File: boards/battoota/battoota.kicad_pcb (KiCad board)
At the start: 2 copper layers, 122.6 x 88.9 mm, 38 parts

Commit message: battoota clean up
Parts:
- removed S10, S12, S14, S16, S18, S20, S22, S24, S28, S30, S32, S34, S4, S6, S8: , PG1350
- S11, S13, S15, S17, S19, S21, S23, S27, S29, S3, S31, S33, S5, S7, S9: footprint PG1350 -> Alaa:choc_hotswap_key
- moved S27 1.72 mm to (133.6, -78.5)
- moved S29 1.72 mm to (133.6, -95.5)
- moved S19 1.61 mm to (115.4, -71.1)
- moved S21 1.61 mm to (115.4, -88.1)
- moved S23 1.61 mm to (115.4, -105.1)
- moved REF** 1.50 mm to (103.8, -86.6)
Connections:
- S11 pad : P3 -> (no net)
- S13 pad : P2 -> (no net)
- S27 pad : P19 -> (no net)
- S29 pad : P20 -> (no net)
- S7 pad : P5 -> (no net)
- S9 pad : P4 -> (no net)
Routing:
- net P2: track 131.6 -> 134.3 mm
- net P15: track 150.2 -> 152.9 mm
- net P18: track 136.7 -> 139.4 mm
- net P16: track 96.8 -> 95.1 mm
- net P20: track 43.9 -> 45.6 mm
- net P10: track 109.7 -> 108.1 mm
- net P7: track 159.0 -> 160.5 mm
- net P6: track 178.1 -> 179.6 mm
- net P4: track 152.4 -> 153.9 mm
- net P3: track 172.1 -> 173.6 mm
- net P5: track 141.4 -> 142.9 mm
- net P19: track 57.7 -> 58.9 mm
- added copper zone on F.Cu, net (none)

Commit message: clean up all the boards
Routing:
- net GND: track 286.0 -> 30.6 mm
- added copper zone on F.Cu, net GND
- removed copper zone on F.Cu, net (none)
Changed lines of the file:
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@@
   (segment (start 47.655954 -88.184596) (end 48.856953 -86.983597) (width 0.25) (layer "B.Cu") (net 1))
   (segment (start 48.856953 -86.983597) (end 48.856953 -78.356283) (width 0.25) (layer "B.Cu") (net 1))
-  (segment (start 122.409791 -55.455499) (end 122.889627 -55.935335) (width 0.5) (layer "F.Cu") (net 2))
-  (segment (start 141.459791 -49.809121) (end 143.680465 -52.029795) (width 0.5) (layer "F.Cu") (net 2))
-  (segment (start 108.167264 -73.809781) (end 107.149791 -74.827254) (width 0.5) (layer "F.Cu") (net 2))
-  (segment (start 63.384822 -105.421809) (end 62.586645 -106.219986) (width 0.5) (layer "F.Cu") (net 2))
-  (segment (start 96.21751 -74.301308) (end 89.760656 -74.301308) (width 0.5) (layer "F.Cu") (net 2))
-  (segment (start 133.599495 -89.644491) (end 127.233116 -89.644491) (width 0.5) (layer "F.Cu") (net 2))
-  (segment (start 63.384822 -100.80225) (end 63.384822 -105.421809) (width 0.5) (layer "F.Cu") (net 2))
-  (segment (start 127.872013 -72.644491) (end 125.324495 -75.192009) (width 0.5) (layer "F.Cu") (net 2))
-  (segment (start 75.363653 -82.192969) (end 74.347654 -81.17697) (width 0.5) (layer "F.Cu") (net 2))
-  (segment (start 115.424791 -65.177254) (end 109.829464 -65.177254) (width 0.5) (layer "F.Cu") (net 2))
-  (segment (start 125.324495 -91.553112) (end 125.324495 -99.294491) (width 0.5) (layer "F.Cu") (net 2))
-  (segment (start 108.167264 -66.839454) (end 108.167264 -73.809781) (width 0.5) (layer "F.Cu") (net 2))
-  (segment (start 62.586645 -106.219986) (end 62.586645 -107.001157) (width 0.5) (layer "F.Cu") (net 2))
-  (segment (start 66.26837 -97.918702) (end 63.384822 -100.80225) (width 0.5) (layer "F.Cu") (net 2))
-  (segment (start 74.347654 -81.17697) (end 68.485407 -81.17697) (width 0.5) (layer "F.Cu") (net 2))
-  (segment (start 71.813295 -64.435238) (end 68.490683 -67.75785) (width 0.5) (layer "F.Cu") (net 2))
-  (segment (start 141.459791 -42.698254) (end 141.459791 -49.809121) (width 0.5) (layer "F.Cu") (net 2))
-  (segment (start 89.760656 -74.301308) (end 87.132946 -76.929018) (width 0.5) (layer "F.Cu") (net 2))
-  (segment (start 109.829464 -65.177254) (end 108.167264 -66.839454) (width 0.5) (layer "F.Cu") (net 2))
-  (segment (start 49.917361 -65.987885) (end 48.802762 -67.102484) (width 0.5) (layer "F.Cu") (net 2))
-  (segment (start 59.537571 -60.830584) (end 58.196209 -59.489222) (width 0.5) (layer "F.Cu") (net 2))
-  (segment (start 77.299673 -64.435238) (end 71.813295 -64.435238) (width 0.5) (layer "F.Cu") (net 2))
-  (segment (start 115.424791 -82.177254) (end 108.987449 -82.177254) (width 0.5) (layer "F.Cu") (net 2))
-  (segment (start 124.609447 -44.744455) (end 122.409791 -46.944111) (width 0.5) (layer "F.Cu") (net 2))
-  (segment (start 78.315672 -65.451237) (end 77.299673 -64.435238) (width 0.5) (layer "F.Cu") (net 2))
-  (segment (start 58.196209 -59.489222) (end 53.137791 -59.489222) (width 0.5) (layer "F.Cu") (net 2))
-  (segment (start 71.395635 -97.918702) (end 66.26837 -97.918702) (width 0.5) (layer "F.Cu") (net 2))
-  (segment (start 53.137791 -59.489222) (end 49.917361 -62.709652) (width 0.5) (layer "F.Cu") (net 2))
-  (segment (start 115.424791 -99.177254) (end 109.579975 -99.177254) (width 0.5) (layer "F.Cu") (net 2))
-  (segment (start 133.599495 -72.644491) (end 127.872013 -72.644491) (width 0.5) (layer "F.Cu") (net 2))
-  (segment (start 86.601289 -108.171928) (end 86.570217 -108.140856) (width 0.5) (layer "F.Cu") (net 2))
-  (segment (start 93.254215 -108.171928) (end 86.601289 -108.171928) (width 0.5) (layer "F.Cu") (net 2))
-  (segment (start 68.485407 -81.17697) (end 65.538664 -84.123713) (width 0.5) (layer "F.Cu") (net 2))
-  (segment (start 85.651298 -93.599163) (end 85.651298 -100.128683) (width 0.5) (layer "F.Cu") (net 2))
-  (segment (start 65.538664 -84.123713) (end 65.538664 -90.259425) (width 0.5) (layer "F.Cu") (net 2))
-  (segment (start 48.802762 -67.102484) (end 48.802762 -67.639549) (width 0.5) (layer "F.Cu") (net 2))
-  (segment (start 147.315045 -39.848335) (end 144.30971 -39.848335) (width 0.5) (layer "F.Cu") (net 2))
   (segment (start 154.256703 -110.643254) (end 150.44369 -110.643254) (width 0.5) (layer "F.Cu") (net 2))
-  (segment (start 122.409791 -46.944111) (end 122.409791 -55.455499) (width 0.5) (layer "F.Cu") (net 2))
-  (segment (start 108.167264 -74.406264) (end 107.149791 -75.423737) (width 0.5) (layer "F.Cu") (net 2))
-  (segment (start 109.579975 -99.177254) (end 107.14979 -101.607439) (width 0.5) (layer "F.Cu") (net 2))
-  (segment (start 94.735862 -91.236618) (end 88.013843 -91.236618) (width 0.5) (layer "F.Cu") (net 2))
-  (segment (start 48.232895 -75.218284) (end 44.864298 -78.586881) (width 0.5) (layer "F.Cu") (net 2))
-  (segment (start 87.132946 -76.929018) (end 87.132946 -83.193373) (width 0.5) (layer "F.Cu") (net 2))
-  (segment (start 129.187964 -44.744455) (end 124.609447 -44.744455) (width 0.5) (layer "F.Cu") (net 2))
-  (segment (start 88.013843 -91.236618) (end 85.651298 -93.599163) (width 0.5) (layer "F.Cu") (net 2))
-  (segment (start 108.987449 -82.177254) (end 107.149791 -84.014912) (width 0.5) (layer "F.Cu") (net 2))
   (segment (start 154.304587 -110.691138) (end 154.256703 -110.643254) (width 0.5) (layer "F.Cu") (net 2))
-  (segment (start 127.233116 -89.644491) (end 125.324495 -91.553112) (width 0.5) (layer "F.Cu") (net 2))
-  (segment (start 44.864298 -78.586881) (end 44.864298 -82.864875) (width 0.5) (layer "F.Cu") (net 2))
-  (segment (start 86.570217 -108.140856) (end 84.169651 -110.541422) (width 0.5) (layer "F.Cu") (net 2))
-  (segment (start 144.30971 -39.848335) (end 141.459791 -42.698254) (width 0.5) (layer "F.Cu") (net 2))
-  (segment (start 54.567252 -77.087765) (end 52.697771 -75.218284) (width 0.5) (layer "F.Cu") (net 2))
-  (segment (start 72.411634 -98.934701) (end 71.395635 -97.918702) (width 0.5) (layer "F.Cu") (net 2))
-  (segment (start 107.149791 -84.014912) (end 107.14979 -91.827254) (width 0.5) (layer "F.Cu") (net 2))
-  (segment (start 68.490683 -67.75785) (end 68.490683 -73.517693) (width 0.5) (layer "F.Cu") (net 2))
-  (segment (start 52.697771 -75.218284) (end 48.232895 -75.218284) (width 0.5) (layer "F.Cu") (net 2))
-  (segment (start 44.864298 -82.864875) (end 43.832443 -83.89673) (width 0.5) (layer "F.Cu") (net 2))
-  (segment (start 49.917361 -62.709652) (end 49.917361 -65.987885) (width 0.5) (layer "F.Cu") (net 2))
-  (segment (start 129.553156 -45.109647) (end 129.187964 -44.744455) (width 0.5) (layer "F.Cu") (net 2))
-  (segment (start 125.324495 -75.192009) (end 125.324495 -82.294491) (width 0.5) (layer "F.Cu") (net 2))
-  (segment (start 107.14979 -101.607439) (end 107.14979 -108.827254) (width 0.5) (layer "F.Cu") (net 2))
-  (segment (start 84.169651 -110.541422) (end 84.169651 -117.063993) (width 0.5) (layer "F.Cu") (net 2))
   (via (at 154.304587 -110.691138) (size 0.8) (drill 0.4) (layers "F.Cu" "B.Cu") (free) (net 2))
   (segment (start 154.329345 -110.66638) (end 154.352471 -110.643254) (width 0.5) (layer "B.Cu") (net 2))
@@
   (segment (start 135.118406 -112.746869) (end 135.109791 -112.738254) (width 0.5) (layer "B.Cu") (net 20))
   (segment (start 135.118406 -118.676838) (end 135.118406 -112.746869) (width 0.5) (layer "B.Cu") (net 20))
-  (zone (net 0) (net_name "") (layer "F.Cu") (hatch edge 0.508)
+  (zone (net 2) (net_name "GND") (layer "F.Cu") (hatch edge 0.508)
     (connect_pads (clearance 0.508))
     (min_thickness 0.254) (filled_areas_thickness no)
-    (fill yes (thermal_gap 0.508) (thermal_bridge_width 0.508))
+    (fill yes (thermal_gap 0.508) (thermal_bridge_width 0.508) (island_removal_mode 1) (island_area_min 0))
     (polygon
       (pts

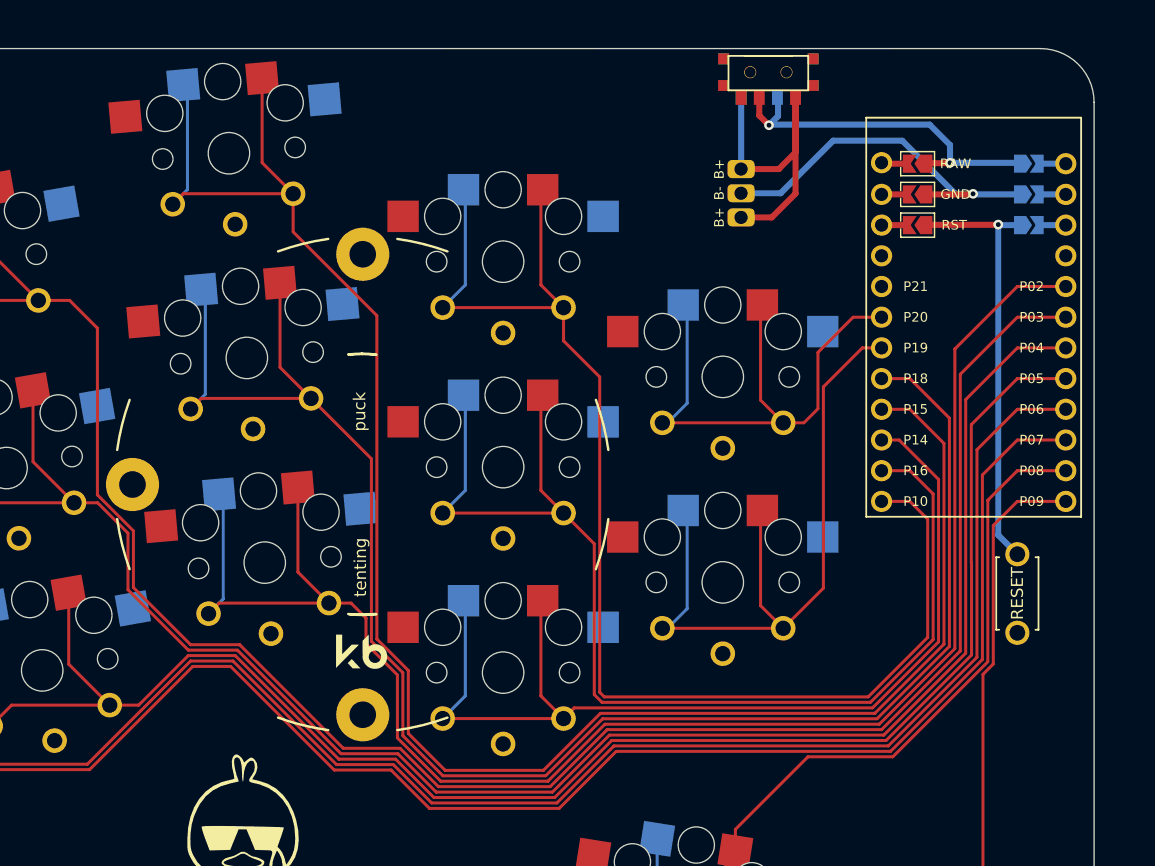
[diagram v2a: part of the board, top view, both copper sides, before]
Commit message: move mcu on battoota up
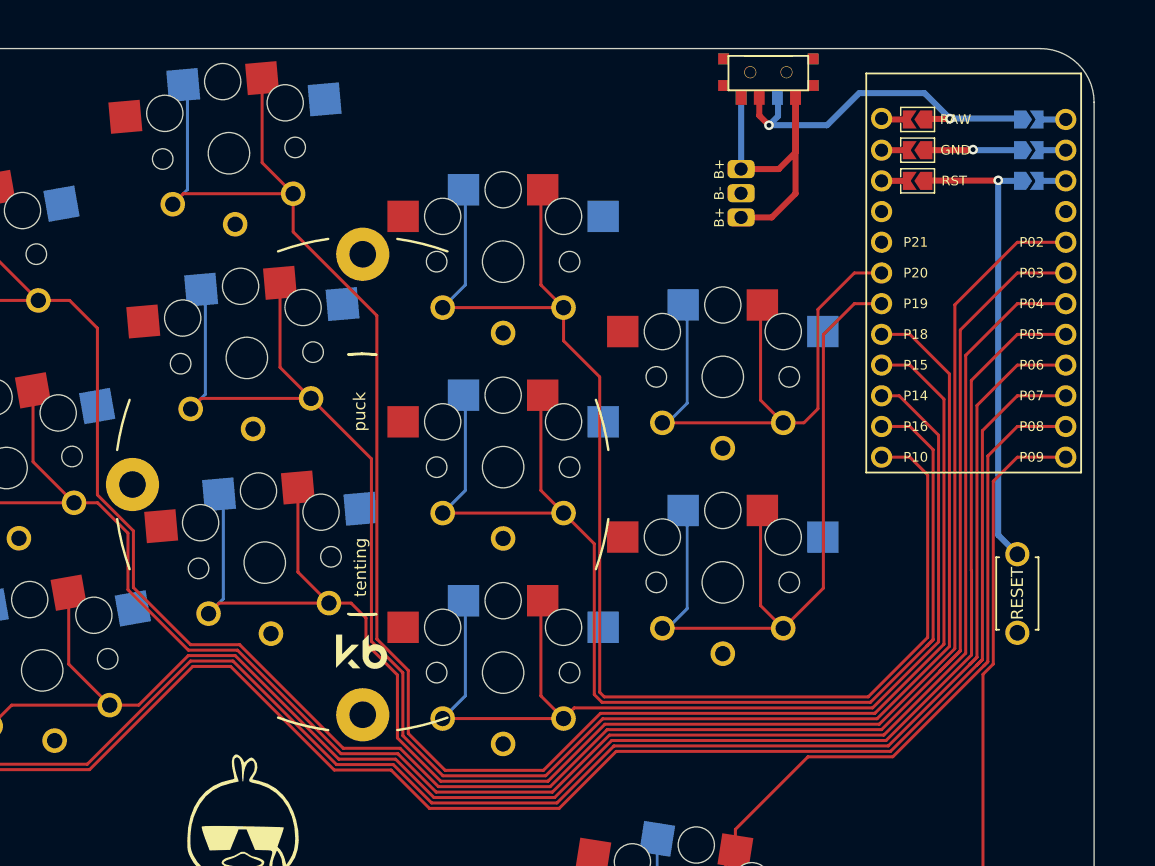
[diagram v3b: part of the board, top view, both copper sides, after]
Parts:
- moved MCU1 3.66 mm to (154.4, -102.9)
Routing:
- net GND: track 30.6 -> 7.75 mm
- net P3: track 173.6 -> 179.7 mm
- net P6: track 179.6 -> 184.0 mm
- net P16: track 95.1 -> 99.5 mm
- net P7: track 160.5 -> 164.9 mm
- net P8: track 81.1 -> 85.3 mm
- net P19: track 58.9 -> 63.0 mm
- net P4: track 153.9 -> 157.5 mm
- net P9: track 73.0 -> 76.7 mm
- net P2: track 134.3 -> 138.0 mm
- net P10: track 108.1 -> 111.8 mm
- net RST: track 35.7 -> 39.4 mm
- net P14: track 84.7 -> 88.3 mm
- net P5: track 142.9 -> 146.5 mm
- net P18: track 139.4 -> 143.1 mm
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
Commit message: min changes
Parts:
- moved G*** 10.0 mm to (103.8, -55.9)
- moved G*** 10.0 mm to (104.0, -55.9)
- moved S31 1.00 mm to (129.5, -50.9)
- moved S33 1.00 mm to (148.7, -45.2)
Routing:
- net P8: track 85.3 -> 88.3 mm
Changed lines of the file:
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@@
   )
   (footprint "LOGO" (layer "F.Cu")
-    (at 93.819755 -55.859733)
+    (at 103.819755 -55.859733)
     (attr board_only exclude_from_pos_files exclude_from_bom)
     (fp_text reference "G***" (at 0 0) (layer "F.SilkS") hide
@@
   )
   (footprint "Alaa:choc_hotswap_key" (layer "F.Cu")
-    (at 149.714791 -45.238254 -24)
+    (at 148.714791 -45.238254 -24)
     (attr through_hole)
     (fp_text reference "S33" (at 0 0 139) (layer "F.SilkS") hide
@@
   )
   (footprint "Alaa:choc_hotswap_key" (layer "F.Cu")
-    (at 130.476118 -50.937009 -9)
+    (at 129.476118 -50.937009 -9)
     (attr through_hole)
     (fp_text reference "S31" (at 0 0 154) (layer "F.SilkS") hide
@@
   )
   (footprint "LOGO" (layer "B.Cu")
-    (at 93.98 -55.88 180)
+    (at 103.98 -55.88 180)
     (attr board_only exclude_from_pos_files exclude_from_bom)
     (fp_text reference "G***" (at 0 0) (layer "B.SilkS") hide
@@
   (segment (start 155.527414 -71.97371) (end 155.191874 -71.638171) (width 0.25) (layer "F.Cu") (net 16))
   (segment (start 161.977213 -91.442348) (end 157.969791 -91.442348) (width 0.25) (layer "F.Cu") (net 16))
-  (segment (start 134.820109 -47.432936) (end 134.820109 -46.401621) (width 0.25) (layer "F.Cu") (net 16))
-  (segment (start 133.839791 -48.413254) (end 134.820109 -47.432936) (width 0.25) (layer "F.Cu") (net 16))
-  (segment (start 125.130937 -47.778254) (end 124.943226 -47.965965) (width 0.25) (layer "F.Cu") (net 16))
+  (segment (start 135.441288 -64.111751) (end 134.641581 -63.312044) (width 0.25) (layer "F.Cu") (net 16))
+  (segment (start 133.820109 -47.432936) (end 133.820109 -46.401621) (width 0.25) (layer "F.Cu") (net 16))
+  (segment (start 132.839791 -48.413254) (end 133.820109 -47.432936) (width 0.25) (layer "F.Cu") (net 16))
+  (segment (start 124.130937 -47.778254) (end 123.943226 -47.965965) (width 0.25) (layer "F.Cu") (net 16))
+  (segment (start 155.191874 -71.638171) (end 147.665453 -64.111751) (width 0.25) (layer "F.Cu") (net 16))
   (segment (start 155.527414 -71.973711) (end 155.191874 -71.638171) (width 0.25) (layer "F.Cu") (net 16))
-  (segment (start 147.665453 -64.111751) (end 140.648288 -64.111751) (width 0.25) (layer "F.Cu") (net 16))
+  (segment (start 134.641581 -63.312044) (end 134.641581 -56.301431) (width 0.25) (layer "F.Cu") (net 16))
   (segment (start 155.527414 -88.999971) (end 155.527414 -71.973711) (width 0.25) (layer "F.Cu") (net 16))
-  (segment (start 134.820109 -46.401621) (end 133.443476 -47.778254) (width 0.25) (layer "F.Cu") (net 16))
-  (segment (start 140.648288 -64.111751) (end 134.641582 -58.105045) (width 0.25) (layer "F.Cu") (net 16))
-  (segment (start 133.443476 -47.778254) (end 125.130937 -47.778254) (width 0.25) (layer "F.Cu") (net 16))
+  (segment (start 133.820109 -46.401621) (end 132.443476 -47.778254) (width 0.25) (layer "F.Cu") (net 16))
+  (segment (start 132.443476 -47.778254) (end 124.130937 -47.778254) (width 0.25) (layer "F.Cu") (net 16))
   (segment (start 134.641583 -56.301431) (end 133.839791 -55.499639) (width 0.25) (layer "F.Cu") (net 16))
-  (segment (start 133.839791 -55.499639) (end 133.839791 -48.413254) (width 0.25) (layer "F.Cu") (net 16))
-  (segment (start 134.641582 -58.105045) (end 134.641582 -56.301432) (width 0.25) (layer "F.Cu") (net 16))
-  (segment (start 155.191874 -71.638171) (end 147.665453 -64.111751) (width 0.25) (layer "F.Cu") (net 16))
+  (segment (start 147.665453 -64.111751) (end 135.441288 -64.111751) (width 0.25) (layer "F.Cu") (net 16))
+  (segment (start 132.839791 -55.499639) (end 132.839791 -48.413254) (width 0.25) (layer "F.Cu") (net 16))
   (segment (start 157.969791 -91.442348) (end 155.527414 -88.999971) (width 0.25) (layer "F.Cu") (net 16))
-  (segment (start 124.943226 -49.041689) (end 124.943226 -47.965965) (width 0.25) (layer "B.Cu") (net 16))
-  (segment (start 128.172224 -52.270687) (end 124.943226 -49.041689) (width 0.25) (layer "B.Cu") (net 16))
-  (segment (start 128.172224 -57.326077) (end 128.172224 -52.270687) (width 0.25) (layer "B.Cu") (net 16))
-  (segment (start 155.976934 -71.787512) (end 155.126735 -70.937314) (width 0.25) (layer "F.Cu") (net 17))
-  (segment (start 152.889791 -39.88597) (end 152.736919 -39.733098) (width 0.25) (layer "F.Cu") (net 17))
-  (segment (start 152.889791 -47.104843) (end 152.889791 -39.88597) (width 0.25) (layer "F.Cu") (net 17))
-  (segment (start 155.976934 -86.909491) (end 155.976934 -71.787512) (width 0.25) (layer "F.Cu") (net 17))
-  (segment (start 150.774947 -39.733098) (end 146.707581 -43.800464) (width 0.25) (layer "F.Cu") (net 17))
-  (segment (start 152.736919 -39.733098) (end 150.774947 -39.733098) (width 0.25) (layer "F.Cu") (net 17))
-  (segment (start 146.707581 -43.800464) (end 143.601465 -43.800464) (width 0.25) (layer "F.Cu") (net 17))
+  (segment (start 123.943226 -49.041689) (end 123.943226 -47.965965) (width 0.25) (layer "B.Cu") (net 16))
+  (segment (start 127.172224 -52.270687) (end 123.943226 -49.041689) (width 0.25) (layer "B.Cu") (net 16))
+  (segment (start 127.172224 -57.326077) (end 127.172224 -52.270687) (width 0.25) (layer "B.Cu") (net 16))
+  (segment (start 151.889791 -39.88597) (end 151.736919 -39.733098) (width 0.25) (layer "F.Cu") (net 17))
   (segment (start 161.977213 -88.902348) (end 157.969791 -88.902348) (width 0.25) (layer "F.Cu") (net 17))
-  (segment (start 155.126735 -70.937314) (end 155.126735 -49.341787) (width 0.25) (layer "F.Cu") (net 17))
+  (segment (start 151.889791 -47.104843) (end 151.889791 -39.88597) (width 0.25) (layer "F.Cu") (net 17))
+  (segment (start 149.774947 -39.733098) (end 145.707581 -43.800464) (width 0.25) (layer "F.Cu") (net 17))
+  (segment (start 155.976934 -51.191986) (end 154.126734 -49.341786) (width 0.25) (layer "F.Cu") (net 17))
+  (segment (start 151.736919 -39.733098) (end 149.774947 -39.733098) (width 0.25) (layer "F.Cu") (net 17))
+  (segment (start 145.707581 -43.800464) (end 142.601465 -43.800464) (width 0.25) (layer "F.Cu") (net 17))
   (segment (start 157.969791 -88.902348) (end 155.976934 -86.909491) (width 0.25) (layer "F.Cu") (net 17))
-  (segment (start 155.126735 -49.341787) (end 152.889791 -47.104843) (width 0.25) (layer "F.Cu") (net 17))
-  (segment (start 149.143013 -52.005911) (end 149.143013 -49.746476) (width 0.25) (layer "B.Cu") (net 17))
-  (segment (start 149.143013 -49.746476) (end 143.601465 -44.204928) (width 0.25) (layer "B.Cu") (net 17))
-  (segment (start 143.601465 -44.204928) (end 143.601465 -43.800464) (width 0.25) (layer "B.Cu") (net 17))
+  (segment (start 154.126735 -49.341787) (end 151.889791 -47.104843) (width 0.25) (layer "F.Cu") (net 17))
+  (segment (start 155.976934 -86.909491) (end 155.976934 -51.191986) (width 0.25) (layer "F.Cu") (net 17))
+  (segment (start 148.143013 -52.005911) (end 148.143013 -49.746476) (width 0.25) (layer "B.Cu") (net 17))
+  (segment (start 148.143013 -49.746476) (end 142.601465 -44.204928) (width 0.25) (layer "B.Cu") (net 17))
+  (segment (start 142.601465 -44.204928) (end 142.601465 -43.800464) (width 0.25) (layer "B.Cu") (net 17))
   (segment (start 152.372041 -116.88499) (end 150.419502 -116.88499) (width 0.5) (layer "F.Cu") (net 18))
   (segment (start 136.618406 -117.166566) (end 137.420433 -116.364539) (width 0.5) (layer "F.Cu") (net 18))
